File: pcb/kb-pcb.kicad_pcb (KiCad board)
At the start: 2 copper layers, 269 x 101.4 mm, 137 parts, among them U1 TEENSY2.0

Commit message: add solder points for pull-down resistors as in #3
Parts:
- added R1: R, Resistors_Universal:Resistor_SMD+THTuniversal_0805to2512_RM10_HandSoldering, B.Cu at (186.1, 92.1)
- added R10: R, Resistors_Universal:Resistor_SMD+THTuniversal_0805to2512_RM10_HandSoldering, B.Cu at (358.1, 92.1)
- added R11: R, Resistors_Universal:Resistor_SMD+THTuniversal_0805to2512_RM10_HandSoldering, B.Cu at (377.2, 92.1)
- added R12: R, Resistors_Universal:Resistor_SMD+THTuniversal_0805to2512_RM10_HandSoldering, B.Cu at (396.2, 92.1)
- added R13: R, Resistors_Universal:Resistor_SMD+THTuniversal_0805to2512_RM10_HandSoldering, B.Cu at (415.3, 92.1)
- added R14: R, Resistors_Universal:Resistor_SMD+THTuniversal_0805to2512_RM10_HandSoldering, B.Cu at (415.3, 112.4)
- added R2: R, Resistors_Universal:Resistor_SMD+THTuniversal_0805to2512_RM10_HandSoldering, B.Cu at (205.7, 92.1)
- added R3: R, Resistors_Universal:Resistor_SMD+THTuniversal_0805to2512_RM10_HandSoldering, B.Cu at (224.8, 92.1)
- added R4: R, Resistors_Universal:Resistor_SMD+THTuniversal_0805to2512_RM10_HandSoldering, B.Cu at (243.8, 92.1)
- added R5: R, Resistors_Universal:Resistor_SMD+THTuniversal_0805to2512_RM10_HandSoldering, B.Cu at (262.9, 92.1)
- added R6: R, Resistors_Universal:Resistor_SMD+THTuniversal_0805to2512_RM10_HandSoldering, B.Cu at (281.9, 92.1)
- added R7: R, Resistors_Universal:Resistor_SMD+THTuniversal_0805to2512_RM10_HandSoldering, B.Cu at (301.0, 92.1)
- added R8: R, Resistors_Universal:Resistor_SMD+THTuniversal_0805to2512_RM10_HandSoldering, B.Cu at (320.0, 92.1)
- added R9: R, Resistors_Universal:Resistor_SMD+THTuniversal_0805to2512_RM10_HandSoldering, B.Cu at (339.1, 92.1)
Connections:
- U1 pad 14: (no net) -> Net-(U1-Pad14)
- U1 pad 29: (no net) -> Net-(U1-Pad29)
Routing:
- net Net-(D14-Pad2): track 443.9 -> 461.7 mm
- net Net-(D16-Pad2): track 94.6 -> 102.1 mm
- net Net-(D1-Pad2): track 108.0 -> 115.3 mm
- net Net-(D21-Pad2): track 273.2 -> 279.6 mm
- net Net-(D13-Pad2): track 421.4 -> 427.8 mm
- net Net-(D12-Pad2): track 395.5 -> 401.9 mm
- net Net-(D22-Pad2): track 205.3 -> 211.8 mm
- net Net-(D18-Pad2): track 132.2 -> 138.6 mm
- net Net-(D10-Pad2): track 236.8 -> 243.3 mm
- net Net-(D23-Pad2): track 197.5 -> 204.0 mm
- net Net-(D20-Pad2): track 151.2 -> 157.7 mm
- net Net-(D19-Pad2): track 158.1 -> 164.6 mm
- net Net-(D17-Pad2): track 106.9 -> 113.4 mm
- net Net-(D11-Pad2): track 370.7 -> 377.2 mm

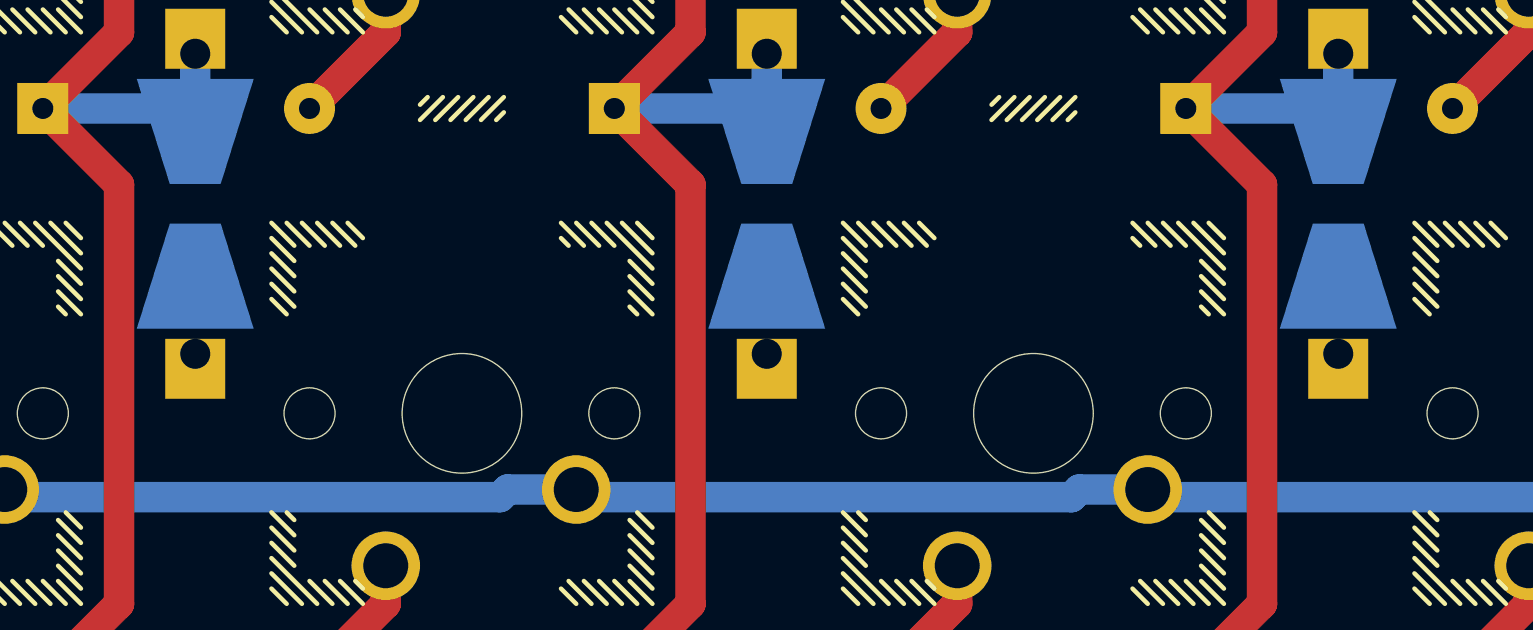
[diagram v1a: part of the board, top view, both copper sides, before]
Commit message: fix two unconnected resistors
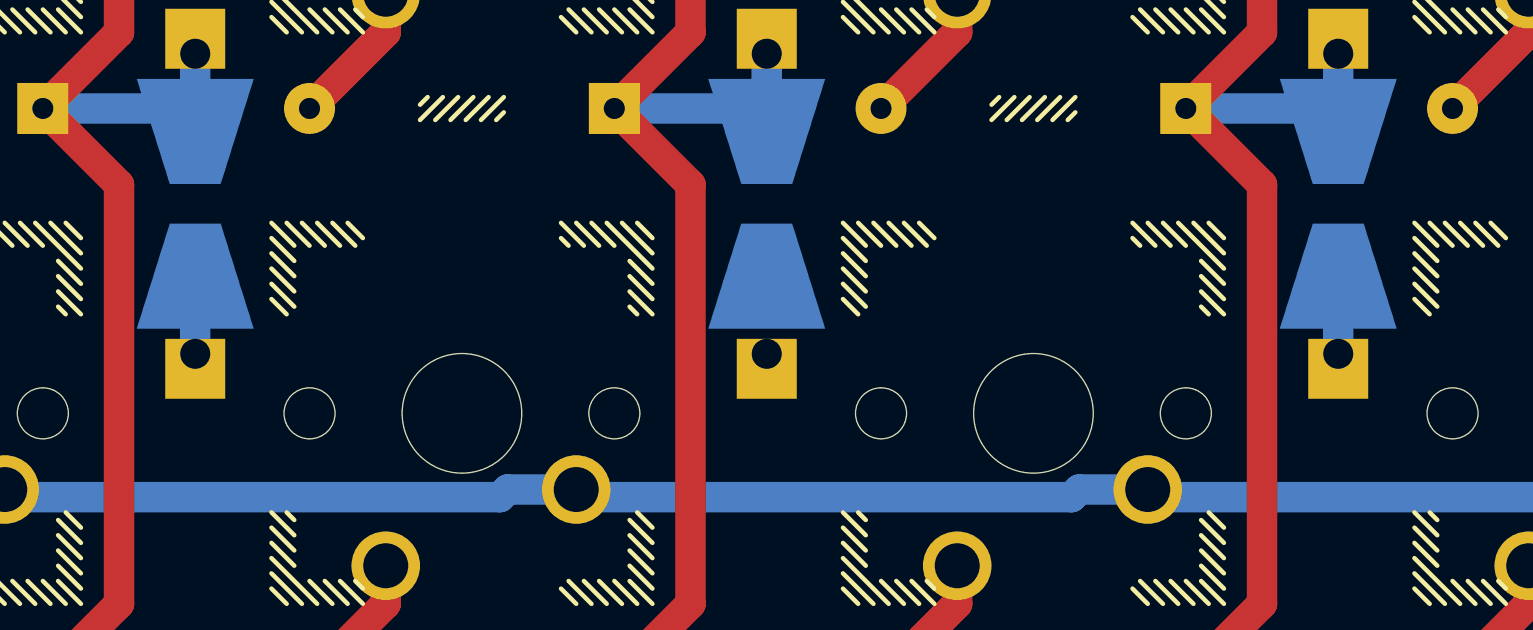
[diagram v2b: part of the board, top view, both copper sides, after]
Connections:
- R7 pad 2: Net-(R7-Pad2) -> /GND
- R9 pad 2: Net-(R9-Pad2) -> /GND
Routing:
- net /GND: track 0.00 -> 5.18 mm
